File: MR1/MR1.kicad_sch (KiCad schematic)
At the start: 14 parts

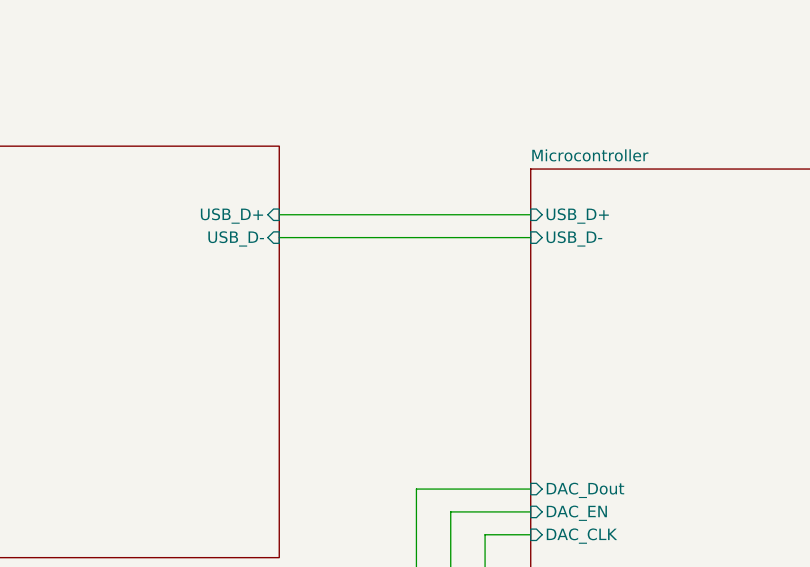
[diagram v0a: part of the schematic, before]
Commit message: feat(cad,firmware,interposer): PTFE interposer, deliverables pipeline, and firmware
- CAD & Interposer:
  - Modeled PTFE_Interposer (55.0 x 51.962 x 0.8 mm) with central wafer diamond cutout
  - Dual-sided silver chloride (Ag/AgCl) ribbon electrode pads (30 deg Cis, 210 deg Trans)
  - 6-pad pogo pin landing array and 4 fluidic pass-throughs with weep duct relief
  - Verified 0 physical collisions across cartridge stack and housings (100% green)
- Deliverables & Export Pipeline:
  - Created automated export system (Makefile, scripts/export_manager.py, scripts/export_all.sh)
  - Full cataloging of 159 deliverables (30 STLs, 13 DXFs, STEPs, Gerbers, WireViz)
  - Added E2E tests (tests/test_exports_e2e.py) and legacy parity tests (tests/test_legacy_feature_parity.py)
- Firmware & Schematics:
  - ESP32-S3 firmware with 100 kHz USB streaming, FreeRTOS dual-core tasks, Web UI
  - Added fast AD40xx SPI driver, MCP4822 DAC driver, leak detection, and pump UART
  - SBU auto-polarity detection and I2C routing in MR1 schematics
- Docs & Environment:
  - Added setup_env.sh, setup_env.ps1, requirements.txt, EXPORTS.md
  - Updated README.md, TODO.md, atlas.project.json, and walkthrough.md
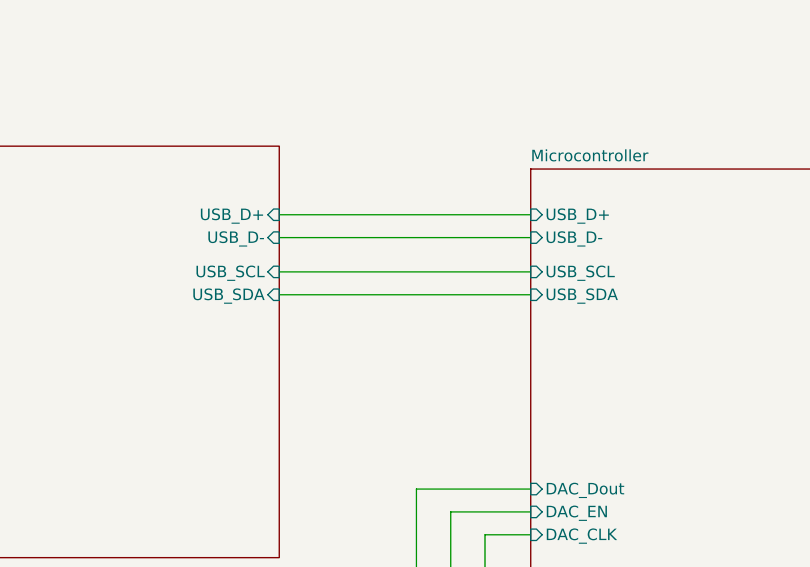
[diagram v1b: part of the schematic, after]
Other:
- sheet Microcontroller ports: added USB_SCL, USB_SDA; removed none
- sheet Power ports: added USB_SCL, USB_SDA; removed none
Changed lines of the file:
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@@
+	(wire
+		(pts
+			(xy 81.28 44.45) (xy 109.22 44.45)
+		)
+		(stroke
+			(width 0)
+			(type default)
+		)
+	)
 	(wire
 		(pts
@@
 		(pts
 			(xy 226.06 140.97) (xy 232.41 140.97)
+		)
+		(stroke
+			(width 0)
+			(type default)
+		)
+	)
+	(wire
+		(pts
+			(xy 81.28 46.99) (xy 109.22 46.99)
 		)
 		(stroke
@@
 			)
 		)
+		(pin "USB_SCL" input
+			(at 81.28 44.45 0)
+			(effects
+				(font
+					(size 1.27 1.27)
+				)
+				(justify right)
+			)
+		)
+		(pin "USB_SDA" input
+			(at 81.28 46.99 0)
+			(effects
+				(font
+					(size 1.27 1.27)
+				)
+				(justify right)
+			)
+		)
 		(instances
 			(project "MR1"
@@
 			(effects
 				(font
+					(size 1.27 1.27)
+				)
+				(justify left)
+			)
+		)
+		(pin "USB_SCL" input
+			(at 109.22 44.45 180)
+			(effects
+				(font
+					(size 1.27 1.27)
+				)
+				(justify left)
+			)
+		)
+		(pin "USB_SDA" input
+			(at 109.22 46.99 180)
+			(effects
+				(font

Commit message: commiting pcb changes
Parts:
- removed H2, H3, H4, H5: MountingHole_Pad, MountingHole:MountingHole_6mm_Pad_Via, symbol Mechanical:MountingHole_Pad
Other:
- sheet Insturmentation ports: added ADC_CLK, ADC_EN, ADC_SDI, ADC_SDO; removed DAC_CLK, DAC_Dout, DAC_EN
- sheet Microcontroller ports: added ADC_CLK, ADC_EN, ADC_SDI, ADC_SDO; removed DAC_CLK, DAC_Dout, DAC_EN

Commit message: updated board, and worked to improve the project, added .agents which might be a mistake, along with the board updates
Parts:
- E1, E2: footprint (none) -> Jumper:SolderJumper-2_P1.3mm_Open_TrianglePad1.0x1.5mm
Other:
- note added: "Error: Cannot add SW1 (footprint 'Custom Footprints:SW_SPST_6mm_gull wing' not found). Error: Cannot add E1 (no footprint assigned). Error: Cannot add E2 (no footprint assigned). Error: Cannot add C40 (no footprint assigned). Error: Cannot add SW2 (footprint 'Custom Footprints:SW_SPST_6mm_gull wing' not found). Error: Cannot add C42 (no footprint assigned). Total warnings: 10, errors: 6."
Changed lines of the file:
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@@
+		)
+	)
+	(text "Error: Cannot add SW1 (footprint 'Custom Footprints:SW_SPST_6mm_gull wing' not found).\nError: Cannot add E1 (no footprint assigned).\nError: Cannot add E2 (no footprint assigned).\nError: Cannot add C40 (no footprint assigned).\nError: Cannot add SW2 (footprint 'Custom Footprints:SW_SPST_6mm_gull wing' not found).\nError: Cannot add C42 (no footprint assigned).\nTotal warnings: 10, errors: 6."
+		(exclude_from_sim no)
+		(at 99.06 168.91 0)
+		(effects
+			(font
+				(size 1.27 1.27)
+			)
 		)
 	)
@@
 			)
 		)
-		(property "Footprint" ""
+		(property "Footprint" "Jumper:SolderJumper-2_P1.3mm_Open_TrianglePad1.0x1.5mm"
 			(at 217.17 126.238 0)
 			(hide yes)
@@
 			)
 		)
-		(property "Footprint" ""
+		(property "Footprint" "Jumper:SolderJumper-2_P1.3mm_Open_TrianglePad1.0x1.5mm"
 			(at 218.44 154.178 0)
 			(hide yes)

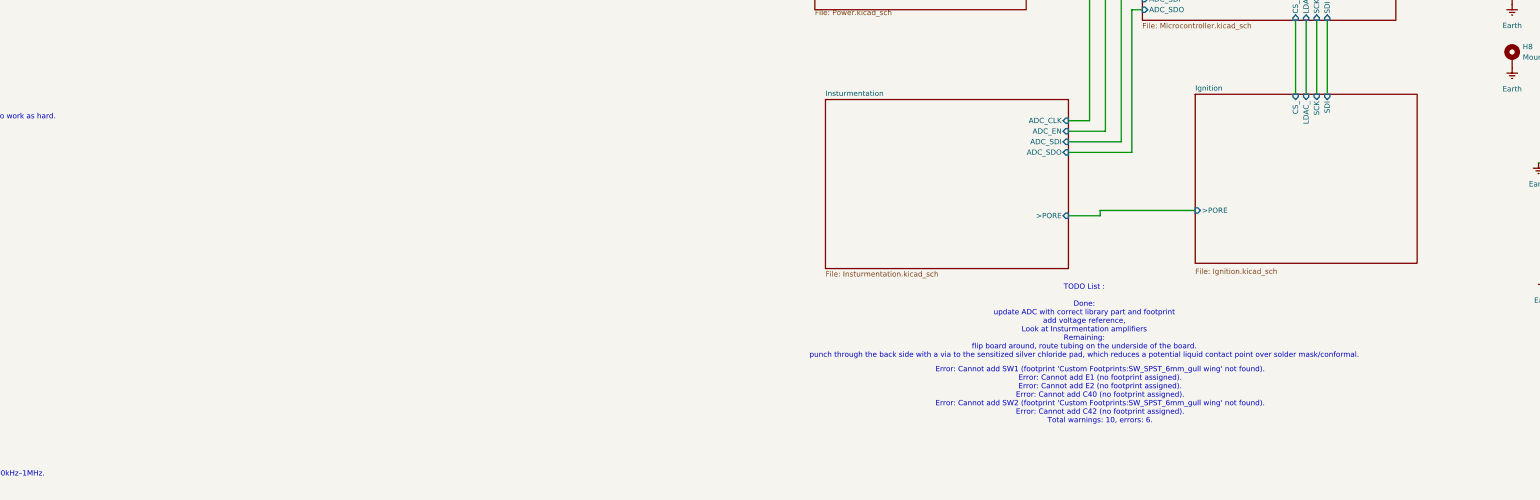
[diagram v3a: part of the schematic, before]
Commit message: chore: prepare repository and documentation for open-source release
- Removed internal .agents scaffolding and updated .gitignore
- Added CONTRIBUTING.md with CAD, PCB, firmware, and PR guidelines
- Added CODE_OF_CONDUCT.md (Contributor Covenant v2.1)
- Added SECURITY.md with hardware safety and vulnerability disclosure policies
- Added CITATION.cff for academic and scientific publications
- Added Pump_firmware/README.md for STM32G431 subsystem
- Expanded BOM.md with mechanical, fluidic, PCB, and active electronics
- Updated README.md test badges, architecture, and documentation index
- Cleared hardcoded absolute developer paths in export_manager.py and KiCad files
- Fixed formatting in install.sh and metadata in package.json
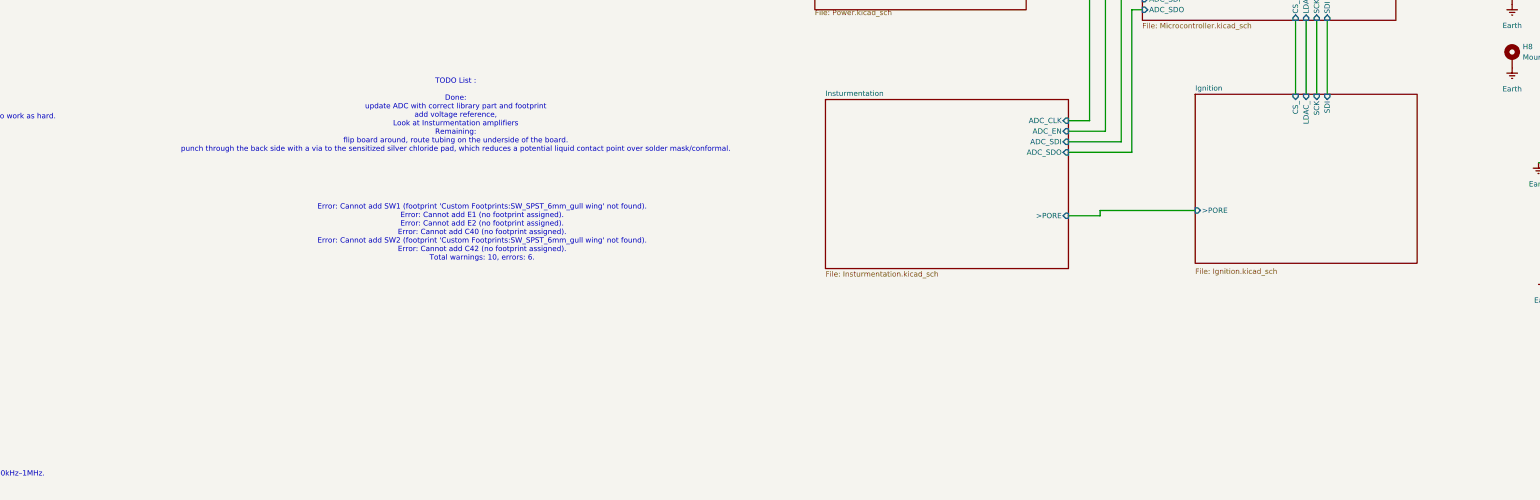
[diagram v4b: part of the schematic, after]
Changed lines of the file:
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@@
 	(text "TODO List :\n\nDone:\nupdate ADC with correct library part and footprint\nadd voltage reference, \nLook at Insturmentation amplifiers\nRemaining:\nflip board around, route tubing on the underside of the board.\npunch through the back side with a via to the sensitized silver chloride pad, which reduces a potential liquid contact point over solder mask/conformal. \n"
 		(exclude_from_sim no)
-		(at 95.25 151.13 0)
+		(at -55.88 101.6 0)
 		(effects
 			(font
@@
 	(text "Error: Cannot add SW1 (footprint 'Custom Footprints:SW_SPST_6mm_gull wing' not found).\nError: Cannot add E1 (no footprint assigned).\nError: Cannot add E2 (no footprint assigned).\nError: Cannot add C40 (no footprint assigned).\nError: Cannot add SW2 (footprint 'Custom Footprints:SW_SPST_6mm_gull wing' not found).\nError: Cannot add C42 (no footprint assigned).\nTotal warnings: 10, errors: 6."
 		(exclude_from_sim no)
-		(at 99.06 168.91 0)
+		(at -49.53 129.794 0)
 		(effects
 			(font

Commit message: lots of refinements.
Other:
- sheet Insturmentation ports: added ROUTE_SEL; removed none
- sheet Microcontroller ports: added ROUTE_SEL; removed none
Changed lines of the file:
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@@
+	(wire
+		(pts
+			(xy 91.44 100.33) (xy 93.98 100.33)
+		)
+		(stroke
+			(width 0)
+			(type default)
+		)
+	)
 	(wire
 		(pts
@@
 	(wire
 		(pts
+			(xy 93.98 66.04) (xy 109.22 66.04)
+		)
+		(stroke
+			(width 0)
+			(type default)
+		)
+	)
+	(wire
+		(pts
 			(xy 210.82 113.03) (xy 204.47 113.03)
 		)
@@
 		(pts
 			(xy 91.44 110.49) (xy 106.68 110.49)
+		)
+		(stroke
+			(width 0)
+			(type default)
+		)
+	)
+	(wire
+		(pts
+			(xy 93.98 100.33) (xy 93.98 66.04)
 		)
 		(stroke
@@
 			)
 		)
+		(pin "ROUTE_SEL" input
+			(at 91.44 100.33 0)
+			(effects
+				(font
+					(size 1.27 1.27)
+				)
+				(justify right)
+			)
+		)
 		(instances
 			(project "MR1"
@@
 			(effects
 				(font
+					(size 1.27 1.27)
+				)
+				(justify left)
+			)
+		)
+		(pin "ROUTE_SEL" input
+			(at 109.22 66.04 180)
+			(effects
+				(font
